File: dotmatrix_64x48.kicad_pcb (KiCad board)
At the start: 2 copper layers, 207 x 120 mm, 393 parts, among them J1 Conn_01x03_Female, J2 Conn_01x03_Male, J3 Micro_SD_Card, J4 Conn_01x06, J7 Conn_01x04_Female, P1 CONN_01X06, P2 CONN_01X06, Q1 AO3401, Q10 AO3401, Q11 AO3401, Q12 AO3401, Q13 AO3401, Q14 AO3401, Q15 AO3401, Q16 AO3401, Q17 AO3401, Q18 AO3401, Q19 AO3401, Q2 Q_NPN_BEC, Q20 AO3401, Q21 AO3401, Q22 AO3401, Q23 AO3401, Q24 AO3401, Q25 AO3401, Q26 AO3401, Q27 AO3401, Q28 AO3401, Q29 AO3401, Q3 NJL7302L-F3, Q30 Q_NPN_BEC, Q4 Q_NPN_BEC, Q5 AO3401, Q6 AO3401, Q7 AO3401, Q8 AO3401, Q9 AO3401, SW1 SW_PUSH_SMALL_H, SW2 SW_PUSH_SMALL_H, SW3 SW_PUSH_SMALL_H, SW4 SW_PUSH_SMALL_H, SW5 SW_PUSH_SMALL_H, SW6 SW_PUSH_SMALL_H, SW7 SW_PUSH_SMALL_H, SW8 SW_PUSH_SMALL_H, T1 COMMON_MODE_CHOKE, U1 74VHC541, U10 LED1642GW, U11 74HC595, U12 AE-BME280, U13 74HC595, U14 TAS5805M, U15 74HC595, U16 ESP32-WROOM, U17 OSRB38C9AA, U18 CM1293A-04SO, U19 TPS54428DDA, U2 TPS54202, U20 CP2102N-A01-GQFN28, U21 CM1293A-04SO, U22 CM1293A-04SO, U23 CM1293A-04SO, U24 CM1293A-04SO, U25 CM1293A-04SO, U26 CM1293A-04SO, U27 CM1293A-04SO, U3 LED1642GW, U4 LED1642GW, U5 LED1642GW, U6 LED1642GW, U7 LED1642GW, U8 LED1642GW, U9 LED1642GW

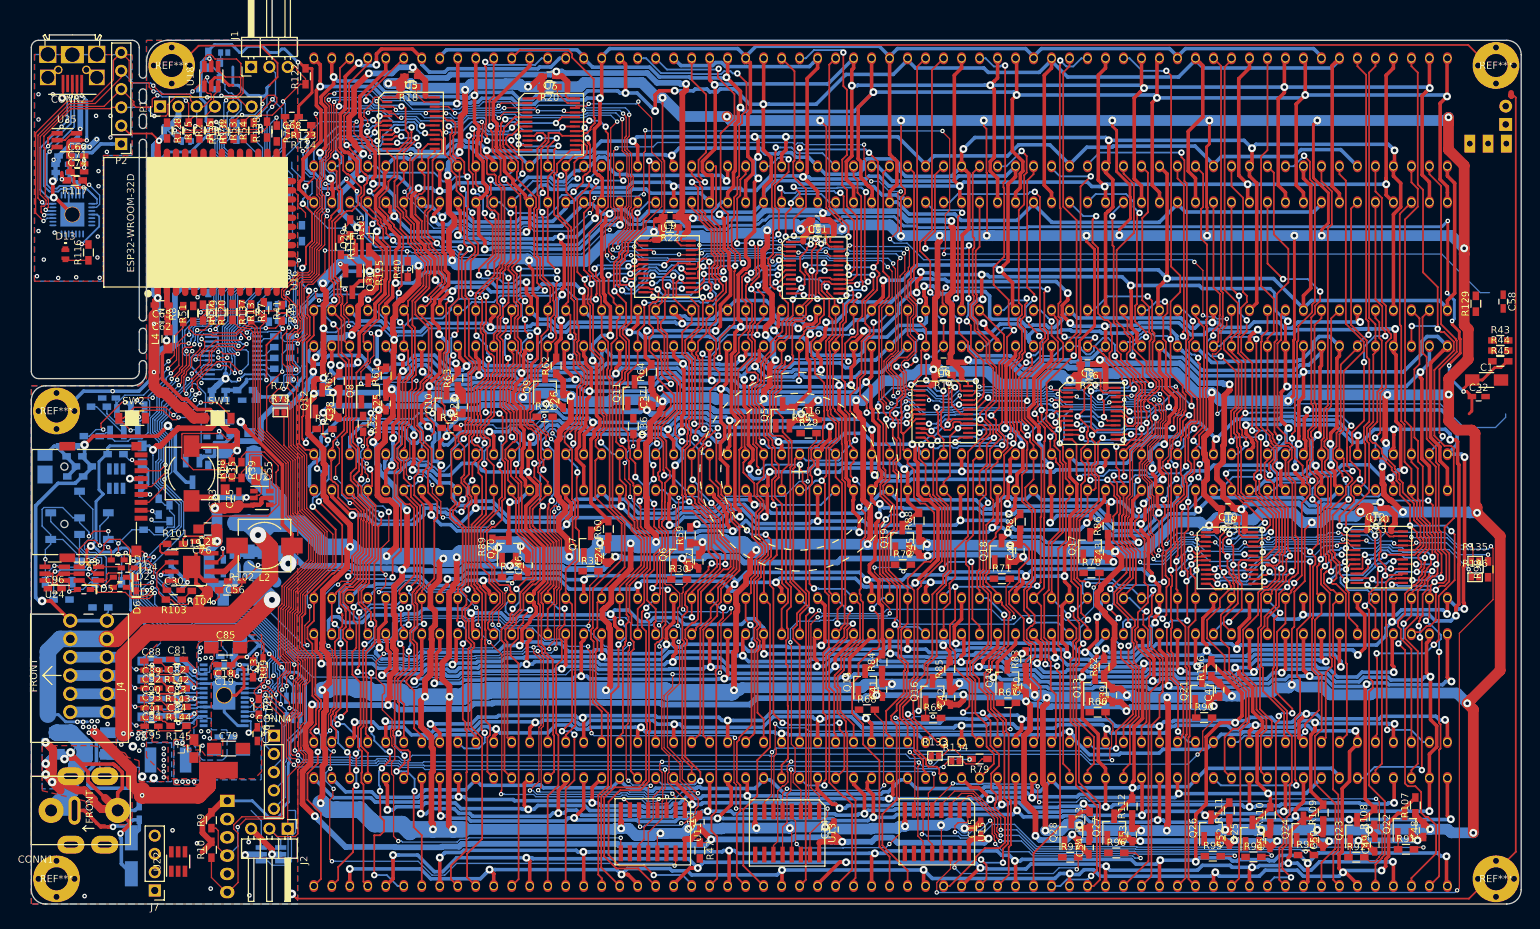
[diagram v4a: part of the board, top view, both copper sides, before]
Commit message: Switched to new kicad libraries
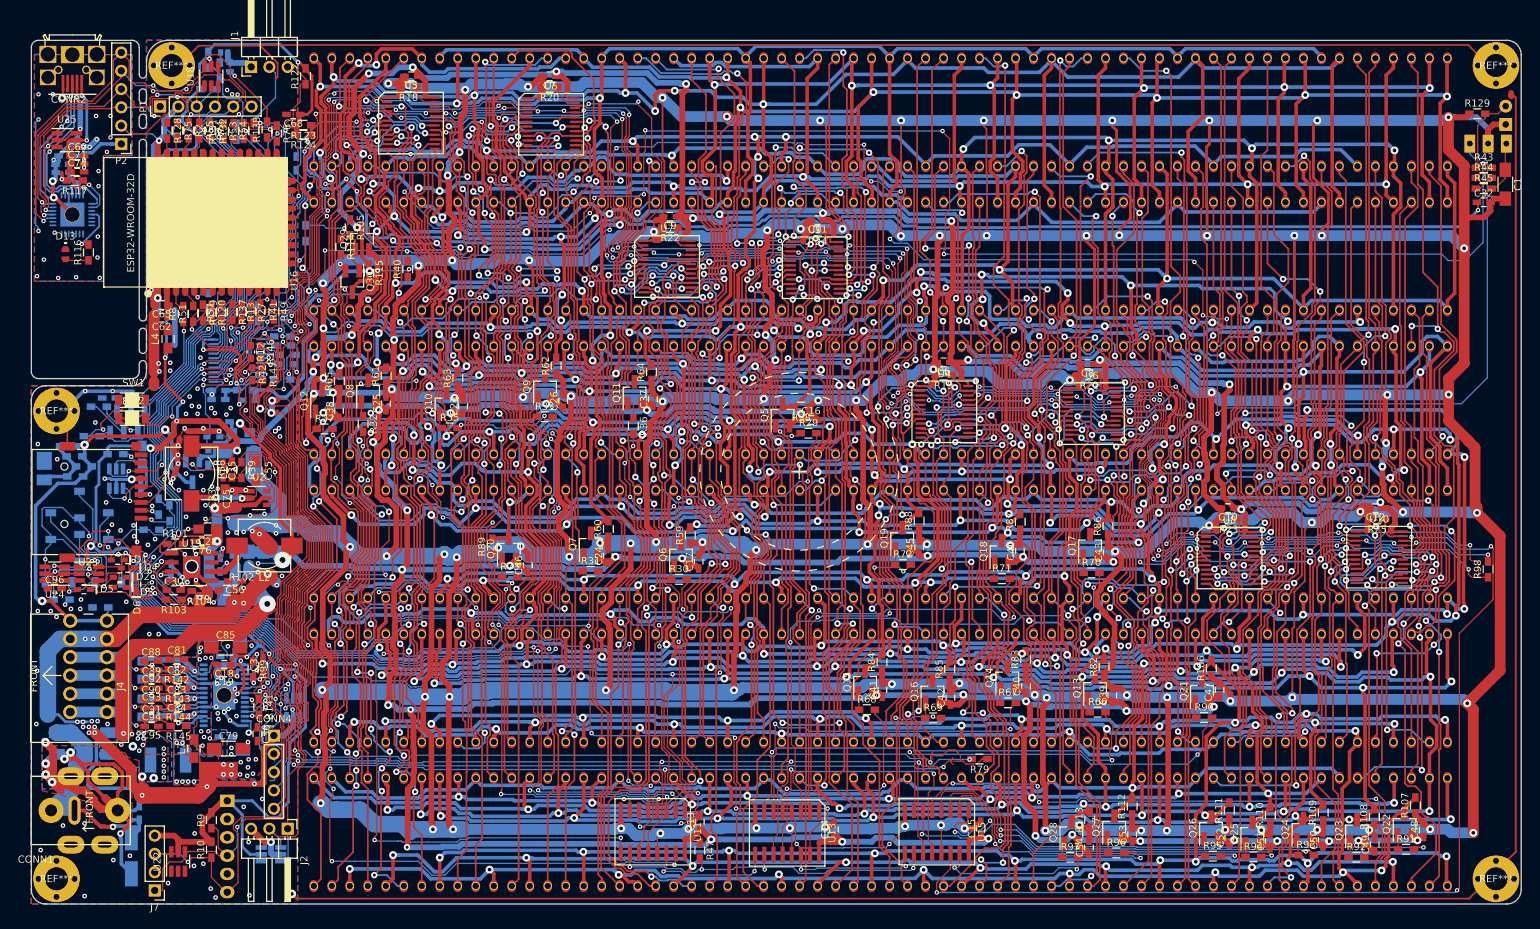
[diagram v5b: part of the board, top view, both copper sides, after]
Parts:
- added R12: 10R, Resistor_SMD:R_0603_1608Metric_Pad1.05x0.95mm_HandSolder, F.Cu at (109.5, 59.3)
- added R146: 10R, Resistor_SMD:R_0603_1608Metric_Pad1.05x0.95mm_HandSolder, F.Cu at (110.8, 59.3)
- added R147: 10R, Resistor_SMD:R_0603_1608Metric_Pad1.05x0.95mm_HandSolder, F.Cu at (111.2, 62.4)
- added R42: 10R, Resistor_SMD:R_0603_1608Metric_Pad1.05x0.95mm_HandSolder, F.Cu at (109.7, 62.4)
- C58: moved to B.Cu
- R133, R134, R135, R136, R77, R78, R80, R81: footprint components:SolderJumper_S -> components:J_0.16mm
- moved C58 168.8 mm to (115.8, 33.1), turned to 90 degrees
- moved C1 27.3 mm to (283.8, 36.0), turned to 270 degrees
- moved C32 27.0 mm to (280.8, 38.5)
- moved R129 26.4 mm to (279.9, 26.2), turned to 0 degrees
- moved R43 24.1 mm to (280.8, 33.7)
- moved R44 24.1 mm to (280.8, 35.1)
- moved R45 24.1 mm to (280.8, 36.6)
- moved SW1 12.2 mm to (93.0, 66.0)
- moved D8 12.0 mm to (106.6, 19.7), turned to 270 degrees
- moved R80 3.86 mm to (113.9, 51.1)
- moved R48 1.50 mm to (110.5, 53.9)
- moved R49 1.12 mm to (112.7, 53.7)
- moved R6 0.86 mm to (114.6, 59.7)
- moved R5 0.84 mm to (114.4, 61.0)
- moved LED49 0.76 mm to (80.8, 75.8), turned to 270 degrees
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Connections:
- R13 pad 2: I2S_SPK_BCLK -> D_I2S_SPK_BCLK
- R137 pad 2: I2S_SPK_MCLK -> D_I2S_SPK_MCLK
- R27 pad 2: I2S_SPK_LRCLK -> D_I2S_SPK_LRCLK
- R41 pad 2: I2S_SPK_DATA -> D_I2S_SPK_DATA
- R6 pad 1: Net-(R6-Pad1) -> Net-(R4-Pad1)
- U1 pad 11: Net-(U1-Pad11) -> Net-(R15-Pad1)
- U1 pad 12: Net-(R15-Pad1) -> Net-(R7-Pad1)
- U1 pad 13: Net-(U1-Pad13) -> Net-(R4-Pad1)
- U1 pad 14: Net-(U1-Pad14) -> Net-(R5-Pad1)
- U1 pad 15: Net-(R7-Pad1) -> Net-(R147-Pad1)
- U1 pad 16: Net-(R6-Pad1) -> Net-(R146-Pad1)
- U1 pad 17: Net-(R5-Pad1) -> Net-(R42-Pad1)
- U1 pad 18: Net-(R4-Pad1) -> Net-(R12-Pad1)
- U1 pad 2: D_COLCLK -> D_I2S_SPK_DATA
- U1 pad 3: D_COLLATCH -> D_I2S_SPK_LRCLK
- U1 pad 4: D_COLCLK -> D_I2S_SPK_BCLK
- U1 pad 5: D_ROW_LAT -> D_I2S_SPK_MCLK
- U1 pad 6: GND -> D_COLSER
- U1 pad 7: GND -> D_ROW_LAT
- U1 pad 8: D_COLSER -> D_COLLATCH
- U1 pad 9: GND -> D_COLCLK
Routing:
- net GND: track 3098.8 -> 3157.6 mm, vias 196 -> 319
- net Net-(R47-Pad2): track 0.00 -> 48.6 mm, vias 0 -> 4
- net E_AIN: track 249.6 -> 282.7 mm, vias 12 -> 13
- net IR_IN: track 254.4 -> 282.5 mm
- net LEDVDD: track 690.6 -> 666.1 mm
- net /IR_Sensor/FILT_VDD: track 217.4 -> 195.5 mm, vias 8 -> 4
- net E_EN: track 40.3 -> 20.8 mm, vias 4 -> 2
- net Net-(U13-Pad14): track 0.00 -> 18.7 mm, vias 0 -> 2
- net Net-(U11-Pad14): track 0.00 -> 18.1 mm, vias 0 -> 2
- net D_COLCLK: track 50.4 -> 36.6 mm, vias 3 -> 1
- net D_COLSER: track 52.1 -> 38.4 mm, vias 5 -> 1
- net Net-(U21-Pad4): track 13.0 -> 0.00 mm
- net D_I2S_SPK_DATA: track 0.00 -> 12.5 mm, vias 0 -> 1
- net SDA: track 151.2 -> 162.6 mm, vias 5 -> 3
- net D_I2S_SPK_LRCLK: track 0.00 -> 11.0 mm, vias 0 -> 1
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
